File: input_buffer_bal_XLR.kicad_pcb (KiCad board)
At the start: 2 copper layers, 75 x 55 mm, 31 parts, among them J1 CH1_XLR, J2 CH2_XLR, J3 POWER, J4 CH1_OUT, J5 CH2_OUT, U1 LM4562, U2 LM4562

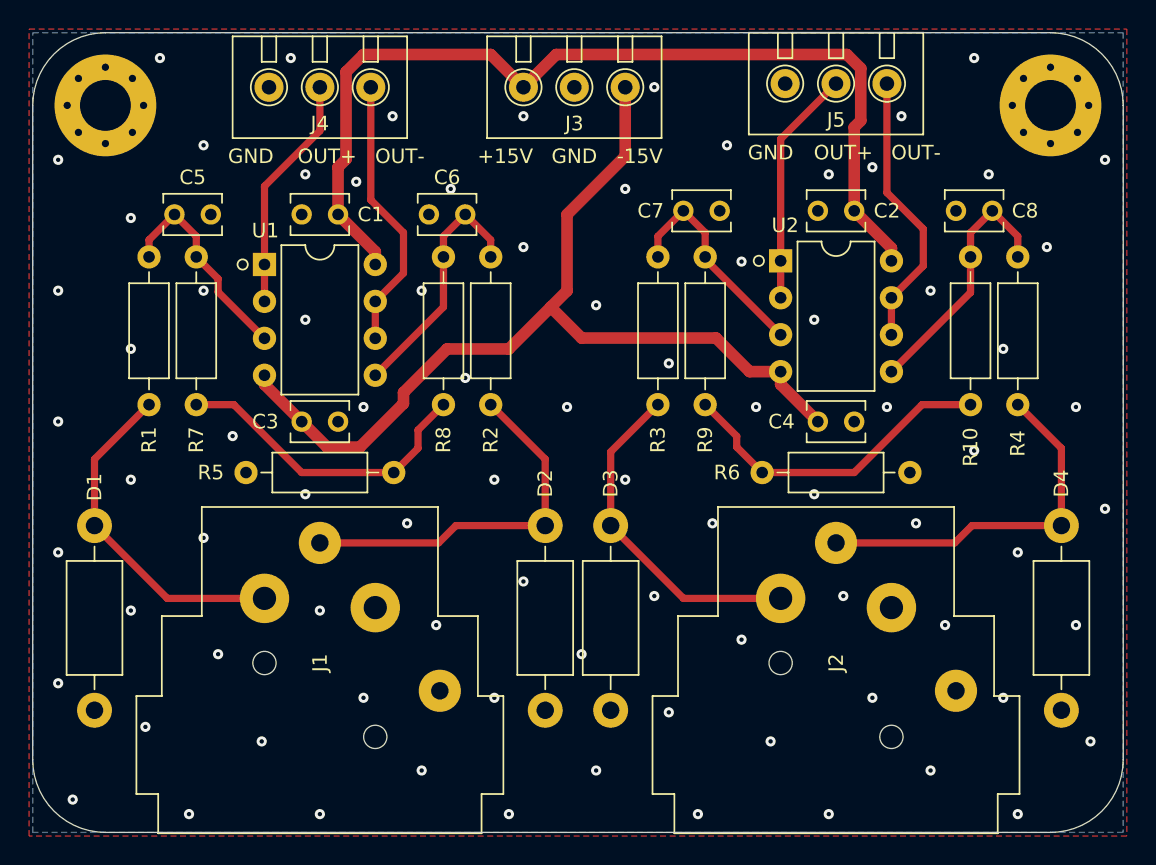
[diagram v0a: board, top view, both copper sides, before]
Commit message: rev1.1 fixes major issues with the layout
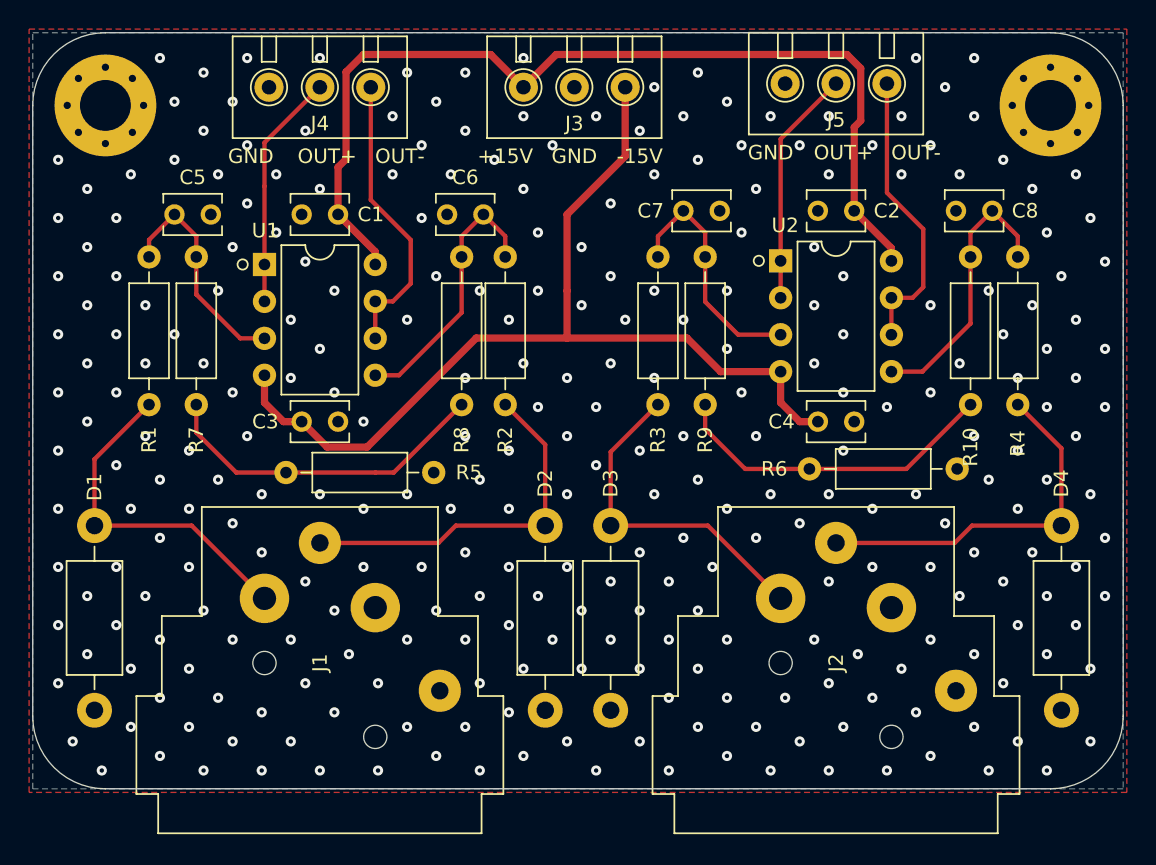
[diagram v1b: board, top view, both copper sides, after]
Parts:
- moved R6 3.26 mm to (143.5, 132.5)
- moved R5 2.75 mm to (107.5, 132.8), turned to 0 degrees
- moved C6 1.25 mm to (114.8, 115.0)
- moved R8 1.25 mm to (114.5, 123.0)
- moved R2 1.00 mm to (117.5, 123.0)
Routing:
- net Net-(C7-Pad1): track 15.2 -> 17.1 mm
- net Net-(R5-Pad1): track 21.6 -> 23.2 mm
- net Net-(C6-Pad2): track 17.3 -> 18.6 mm
- net Net-(C8-Pad2): track 17.8 -> 19.1 mm
- net Net-(J4-Pad1): track 19.0 -> 20.1 mm
- net Net-(C5-Pad1): track 14.7 -> 15.7 mm
- net -15V: track 65.9 -> 66.9 mm
- net Net-(J5-Pad1): track 19.2 -> 20.1 mm
- net GND: vias 84 -> 292
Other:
- board size 75 x 55 mm -> 75 x 52 mm
- board text added: "May 2023"
- board text added: "Rev1.1"

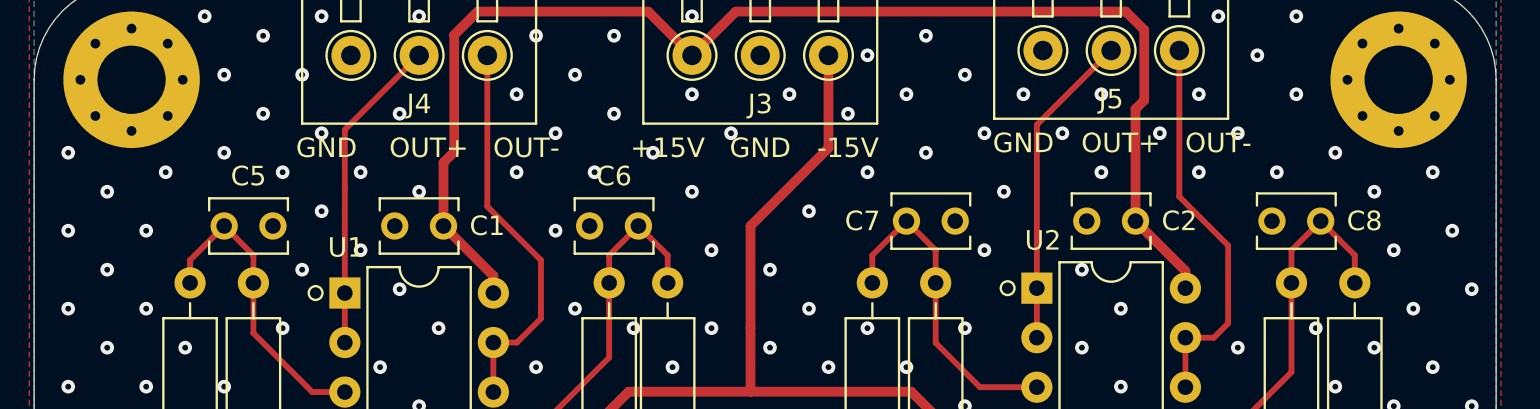
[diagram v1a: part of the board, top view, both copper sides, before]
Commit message: updates to film caps
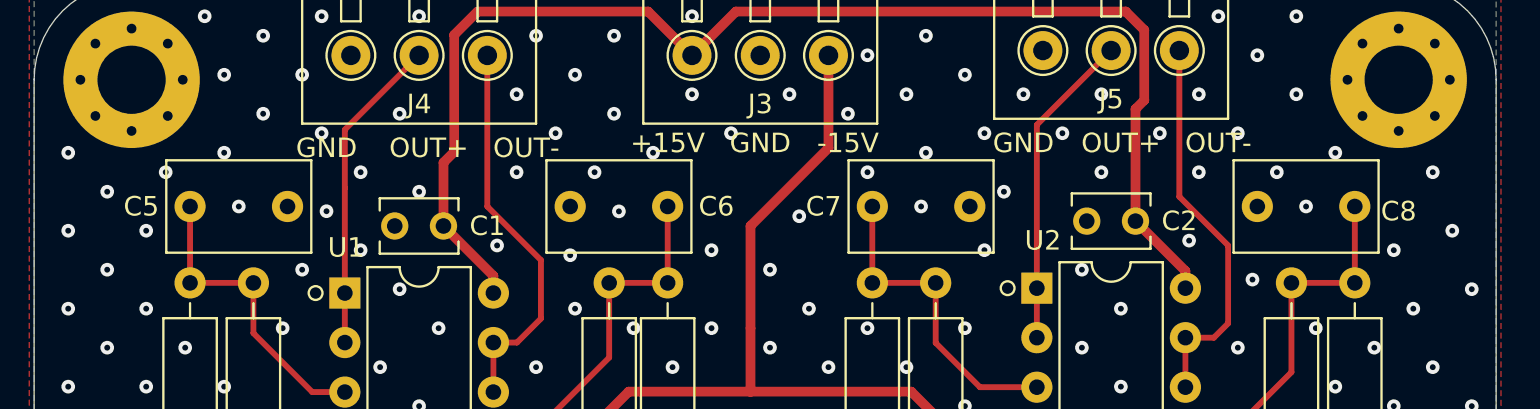
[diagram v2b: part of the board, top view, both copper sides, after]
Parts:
- C5, C6, C7, C8: footprint local_footprint_lib:C_Disc_D3.8mm_W2.6mm_P2.50mm_centered -> Capacitor_THT:C_Rect_L7.2mm_W4.5mm_P5.00mm_FKS2_FKP2_MKS2_MKP2
- moved C5 3.16 mm to (93.0, 114.0)
- moved C7 3.09 mm to (128.0, 114.0)
- moved C6 2.46 mm to (112.5, 114.0)
- moved C8 2.14 mm to (147.8, 114.0)
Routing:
- net Net-(C8-Pad2): track 19.1 -> 18.6 mm
- net Net-(C7-Pad1): track 17.1 -> 16.5 mm
- net GND: vias 292 -> 294
- net (no net): vias 0 -> 2
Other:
- board text added: "Rev1.1f"
- board text removed: "Rev1.1"

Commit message: rev1.2
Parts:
- J3: footprint local_footprint_lib:TerminalBlock_ Amphenol_01_03_P3.50mm -> local_footprint_lib:TerminalBlock_ Amphenol_01_02_P3.50mm
- moved C1 0.25 mm to (104.8, 115.2)
- moved C2 0.25 mm to (140.2, 115.0)
- moved C4 0.25 mm to (140.2, 129.0)
- moved C6 0.25 mm to (112.8, 114.0)
- moved J3 0.25 mm to (122.5, 106.2)
- moved J5 0.25 mm to (140.2, 106.2)
- moved R2 0.25 mm to (117.8, 123.0)
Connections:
- J3 pad 1: -15V -> +15V
- J3 pad 2: GND -> -15V
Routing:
- net -15V: track 66.9 -> 69.5 mm
- net +15V: track 67.2 -> 69.5 mm
- net GND: vias 294 -> 303
- net (no net): vias 2 -> 0
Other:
- board text added: "Rev1.2f"
- board text removed: "Rev1.1f"

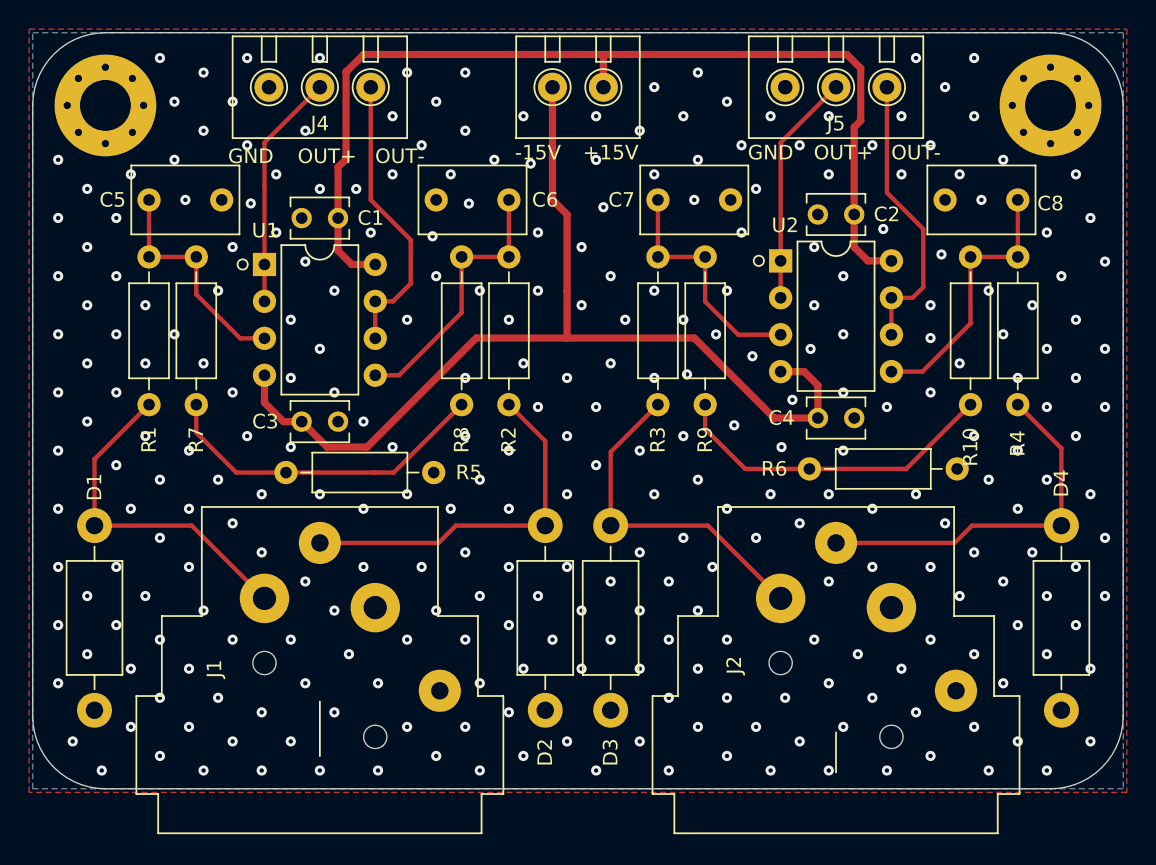
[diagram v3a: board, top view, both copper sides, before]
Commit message: updated to r2.0
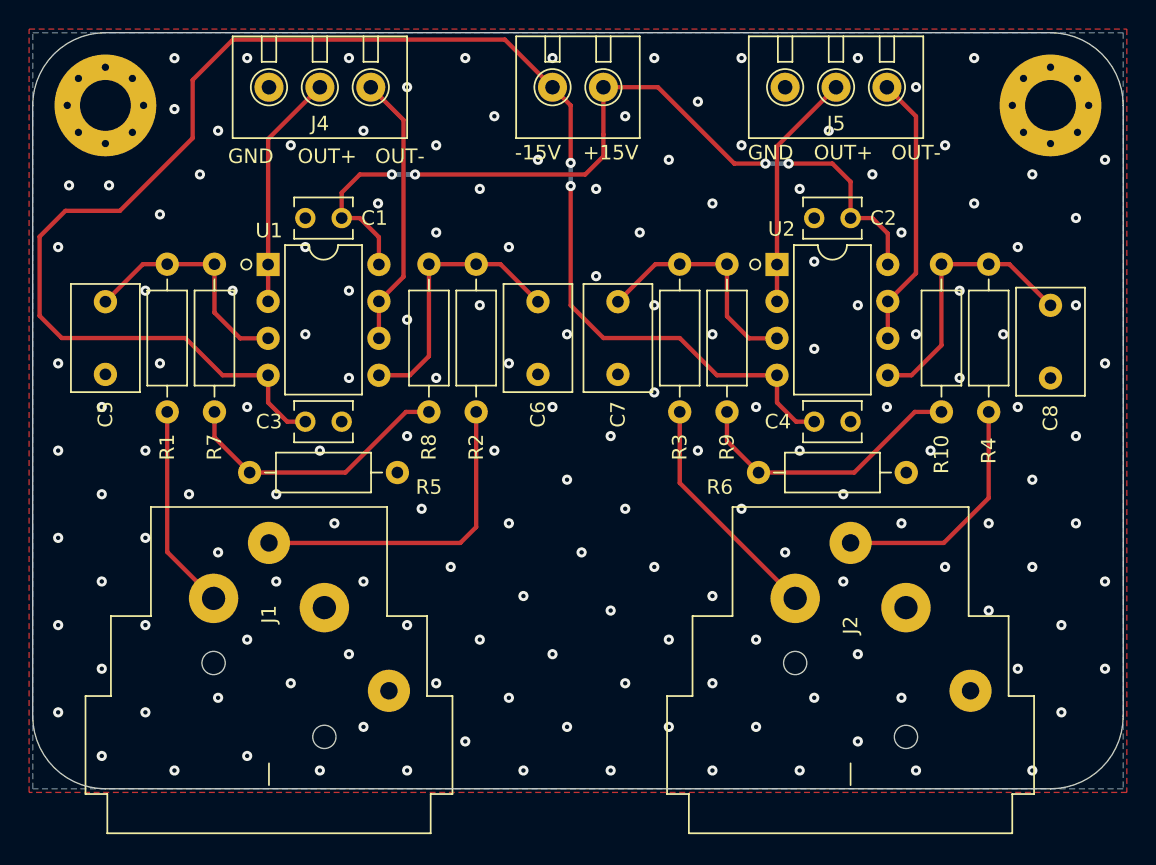
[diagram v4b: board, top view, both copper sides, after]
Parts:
- removed D1, D2, D3, D4: P6KE6.8, local_footprint_lib:D_DO-15_P12.70mm_Horizontal_centered_TVS
- moved C8 14.2 mm to (155.0, 126.2), turned to 90 degrees
- moved C6 13.9 mm to (119.8, 126.0), turned to 90 degrees
- moved C5 7.62 mm to (90.0, 121.0), turned to 270 degrees
- moved C7 7.52 mm to (125.2, 121.0), turned to 270 degrees
- moved R6 3.51 mm to (140.0, 132.8)
- moved J1 3.50 mm to (101.2, 157.5)
- moved R5 2.50 mm to (105.0, 132.8)
- moved R2 2.30 mm to (115.5, 123.5)
- moved R8 2.30 mm to (112.2, 123.5)
- moved R10 2.06 mm to (147.5, 123.5)
- moved R4 2.06 mm to (150.8, 123.5)
- moved R3 1.58 mm to (129.5, 123.5)
- moved R9 1.58 mm to (132.8, 123.5)
- moved R1 1.35 mm to (94.2, 123.5)
- moved R7 1.35 mm to (97.5, 123.5)
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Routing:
- net -15V: track 69.5 -> 109.1 mm, vias 0 -> 2
- net +15V: track 69.5 -> 57.8 mm, vias 0 -> 4
- net Net-(J1-Pad2): track 23.6 -> 14.1 mm
- net Net-(J2-Pad3): track 25.6 -> 16.7 mm
- net Net-(J2-Pad2): track 23.4 -> 16.1 mm
- net Net-(R5-Pad1): track 23.2 -> 19.2 mm
- net Net-(R10-Pad1): track 22.9 -> 19.4 mm
- net Net-(J1-Pad3): track 25.3 -> 22.6 mm
- net Net-(J4-Pad1): track 20.1 -> 18.9 mm
- net Net-(J5-Pad1): track 19.8 -> 18.9 mm
- net Net-(C5-Pad1): track 15.7 -> 16.3 mm
- net GND: vias 303 -> 160
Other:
- board text added: "Rev2.0"
- board text removed: "Rev1.2f"
